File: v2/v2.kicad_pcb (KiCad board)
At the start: 2 copper layers, 9.7 x 8.4 mm, 105 parts, among them J1 Conn_01x04_Pin, J2 Conn_01x04_Pin, J3 Conn_01x04_Pin, SW1 SW_Push, SW10 SW_Push, SW11 SW_Push, SW12 SW_Push, SW13 SW_Push, SW14 SW_Push, SW15 SW_Push, SW16 SW_Push, SW17 SW_Push, SW18 SW_Push, SW19 SW_Push, SW2 SW_Push, SW20 SW_Push, SW21 SW_Push, SW22 SW_Push, SW23 SW_Push, SW24 SW_Push, SW25 SW_Push, SW26 SW_Push, SW27 SW_Push, SW28 SW_Push, SW29 SW_Push, SW3 SW_Push, SW30 SW_Push, SW31 SW_Push, SW32 SW_Push, SW33 RotaryEncoder_Switch, SW4 SW_Push, SW5 SW_Push, SW6 SW_Push, SW7 SW_Push, SW8 SW_Push, SW9 SW_Push, U1 Pico, U2 Pico

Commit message: started running traces
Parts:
- moved U1 4.67 mm to (257.7, 122.0)
- moved U2 4.67 mm to (257.7, 122.0)
- moved J2 4.67 mm to (259.4, 155.9)
- moved J1 4.67 mm to (254.9, 155.7)
- moved R3 4.67 mm to (271.4, 146.1)
- moved R4 4.67 mm to (271.6, 133.7)
- moved J3 3.90 mm to (279.7, 182.8)
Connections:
- D2 pad 1: Net-(D2-K) -> Row 1
- D3 pad 1: Net-(D2-K) -> Row 1
- D4 pad 1: Net-(D2-K) -> Row 1
- D5 pad 1: Net-(D2-K) -> Row 1
- D6 pad 1: Net-(D2-K) -> Row 1
- D7 pad 1: Net-(D2-K) -> Row 1
- U1 pad 31: unconnected-(U1-GPIO26_ADC0-Pad31) -> ENC B
- U1 pad 32: unconnected-(U1-GPIO27_ADC1-Pad32) -> ENC A
- U1 pad 36: unconnected-(U1-3V3-Pad36) -> +3.3V
- U2 pad 24: unconnected-(U2-GPIO18-Pad24) -> SERIAL B
- U2 pad 25: unconnected-(U2-GPIO19-Pad25) -> SERIAL A
- U2 pad 31: unconnected-(U2-GPIO26_ADC0-Pad31) -> ENC B
- U2 pad 32: unconnected-(U2-GPIO27_ADC1-Pad32) -> ENC A
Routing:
- net Row 5: track 0.00 -> 146.9 mm, vias 0 -> 1
- net Row 2: track 0.00 -> 125.6 mm, vias 0 -> 1
- net Row 3: track 0.00 -> 125.3 mm, vias 0 -> 1
- net Row 4: track 0.00 -> 125.1 mm, vias 0 -> 1
- net Col 7: track 0.00 -> 104.7 mm, vias 0 -> 1
- net Col 4: track 0.00 -> 102.4 mm, vias 0 -> 1
- net Col 6: track 0.00 -> 101.8 mm, vias 0 -> 1
- net Row 1: track 0.00 -> 101.0 mm, vias 0 -> 1
- net GND: track 0.00 -> 100.2 mm, vias 0 -> 1
- net Col 2: track 0.00 -> 99.8 mm, vias 0 -> 1
- net Col 5: track 0.00 -> 98.8 mm, vias 0 -> 1
- net Col 3: track 0.00 -> 97.3 mm, vias 0 -> 1
- net Col 1: track 0.00 -> 81.8 mm, vias 0 -> 1
- net +3.3V: track 0.00 -> 47.4 mm, vias 0 -> 1
- net Net-(D6-A): track 0.00 -> 13.8 mm
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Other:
- board size 9.7 x 8.4 mm -> 170.5 x 144.8 mm

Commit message: done for tonight, more trace routing
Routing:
- net Col 1: track 81.8 -> 231.3 mm
- net Col 2: track 99.8 -> 205.2 mm
- net Col 3: track 97.3 -> 185.9 mm
- net Col 4: track 102.4 -> 168.3 mm
- net Col 5: track 98.8 -> 146.0 mm
- net Col 6: track 101.8 -> 122.4 mm
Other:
- outline, holes or cut-outs redrawn

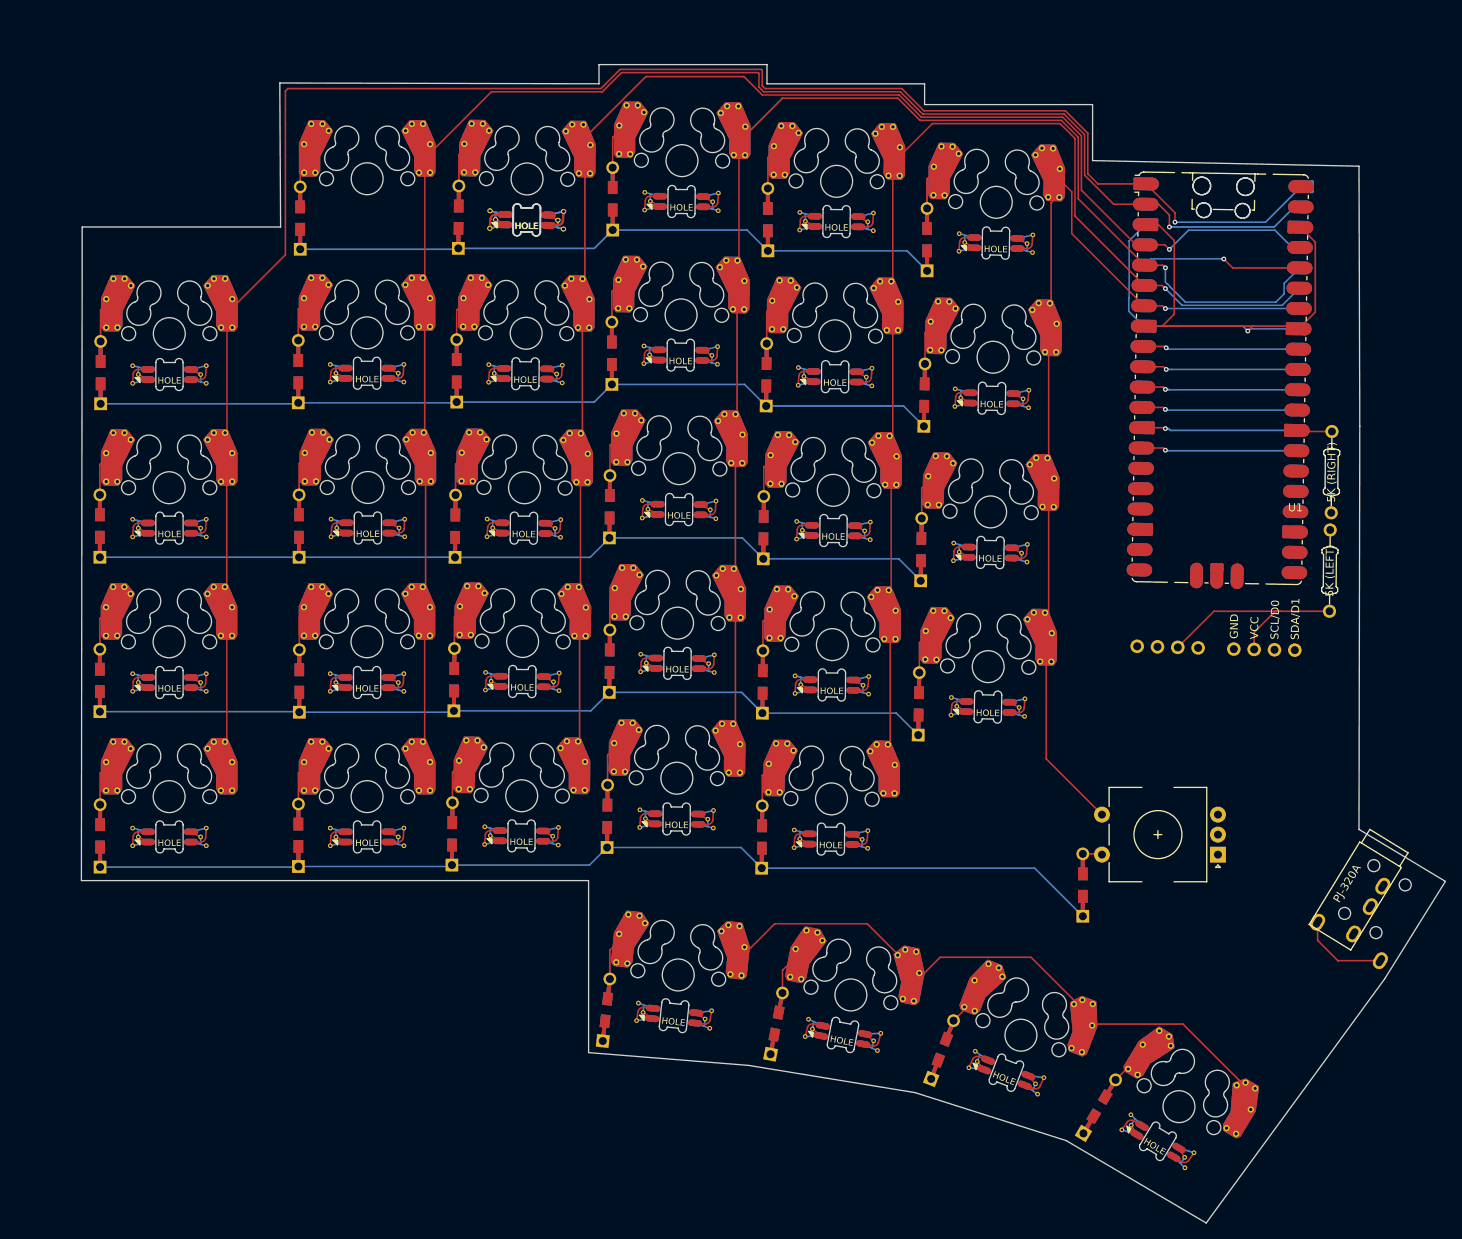
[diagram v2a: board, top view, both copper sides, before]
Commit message: redo some schematics, time to redo LEDs
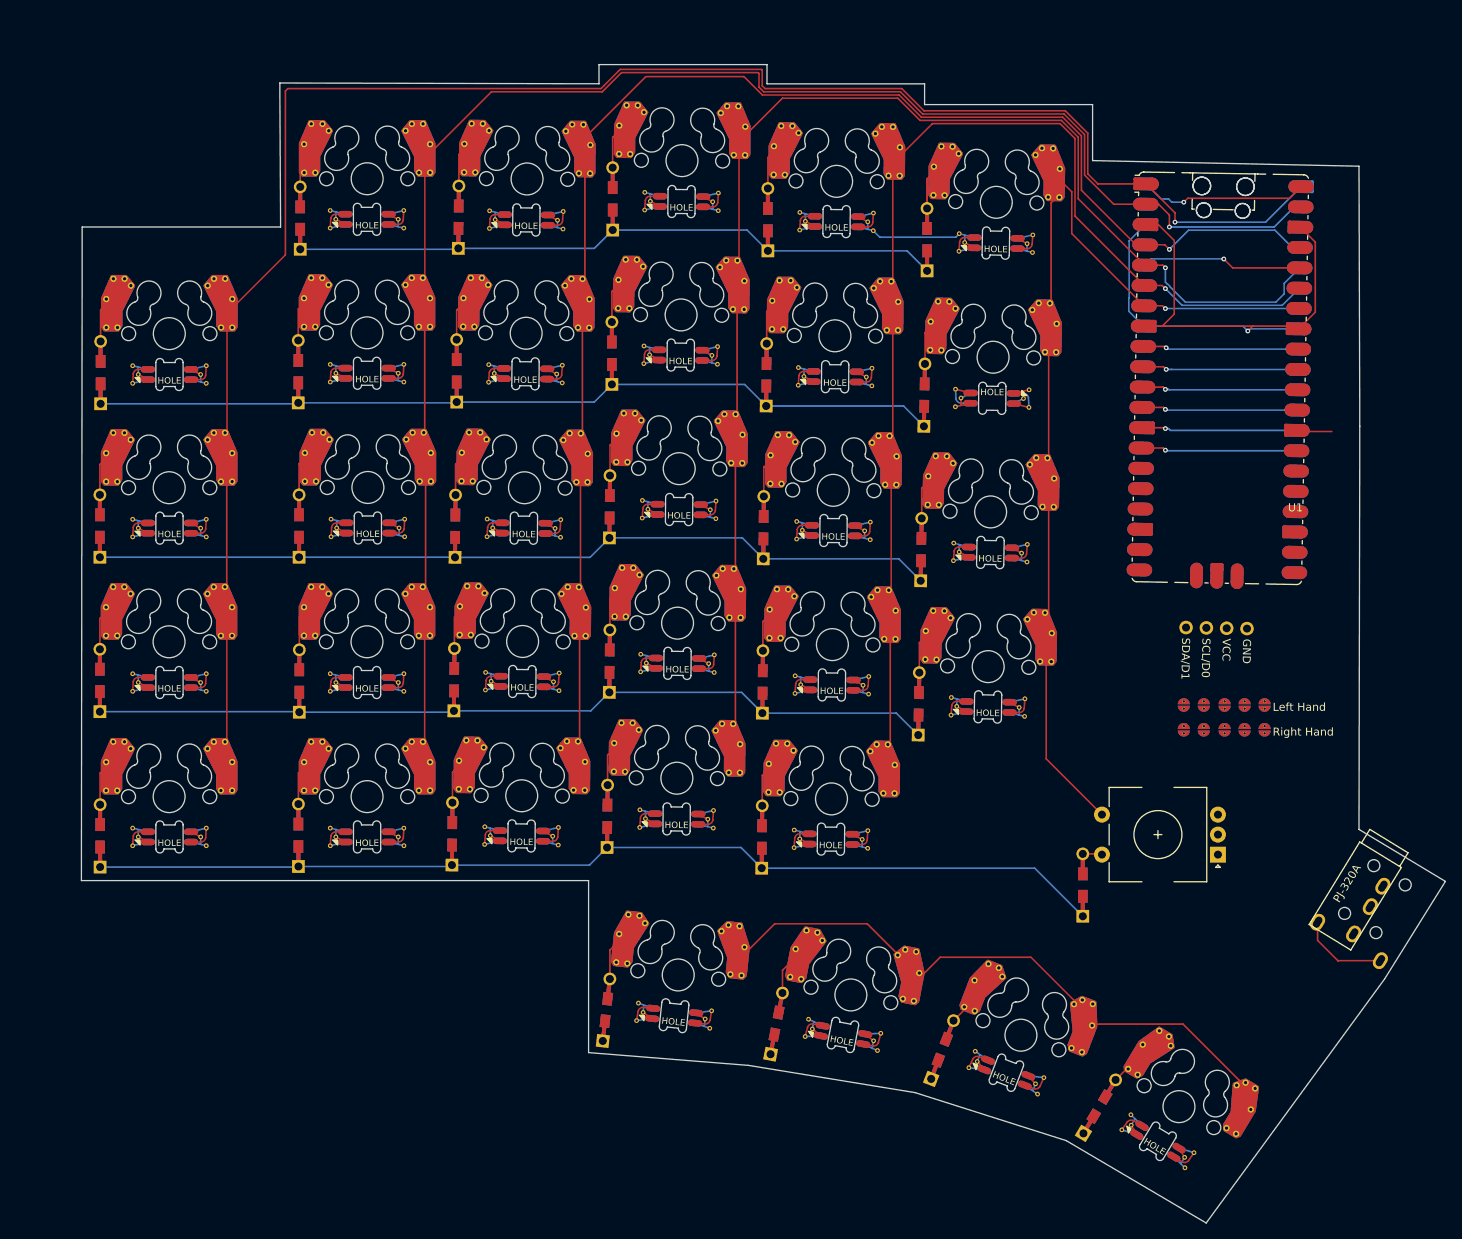
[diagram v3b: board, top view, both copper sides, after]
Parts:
- removed J1: Conn_01x04_Pin, Keebio-Parts:I2C_Breakout
- removed R3: 5K (LEFT), Keebio-Parts:Resistor
- removed R4: 5K (RIGHT), Keebio-Parts:Resistor
- added JP1: GND, Keebio-Parts:solder_jumper, F.Cu at (253.1, 165.9)
- added JP10: Left, Keebio-Parts:solder_jumper, F.Cu at (263.2, 165.9)
- added JP2: VCC, Keebio-Parts:solder_jumper, F.Cu at (255.6, 165.9)
- added JP3: SCL, Keebio-Parts:solder_jumper, B.Cu at (255.6, 162.8)
- added JP4: SDA, Keebio-Parts:solder_jumper, F.Cu at (260.7, 165.9)
- added JP5: SDA, Keebio-Parts:solder_jumper, B.Cu at (253.1, 162.8)
- added JP6: SCL, Keebio-Parts:solder_jumper, F.Cu at (258.2, 165.9)
- added JP7: VCC, Keebio-Parts:solder_jumper, B.Cu at (258.2, 162.8)
- added JP8: GND, Keebio-Parts:solder_jumper, B.Cu at (260.7, 162.8)
- added JP9: Right, Keebio-Parts:solder_jumper, F.Cu at (263.2, 162.8)
- LED13: moved to B.Cu
- moved LED2 20.1 mm to (151.0, 97.1), turned to 0 degrees
- moved J2 3.04 mm to (261.0, 153.3), turned to -91 degrees
- turned LED13 to 179.5 degrees
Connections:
- J2 pad 1: GND -> Net-(J2-Pin_1)
- J2 pad 2: +3.3V -> Net-(J2-Pin_2)
- J2 pad 3: SCL -> Net-(J2-Pin_3)
- J2 pad 4: SCA -> Net-(J2-Pin_4)
- LED30 pad 1: unconnected-(LED30-DOUT-Pad1) -> Net-(LED30-DOUT)
- LED31 pad 3: unconnected-(LED31-DIN-Pad3) -> Net-(LED30-DOUT)
- U1 pad 26: unconnected-(U1-GPIO20-Pad26) -> SDA
- U1 pad 27: unconnected-(U1-GPIO21-Pad27) -> SDL
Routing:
- net +3.3V: track 47.4 -> 20.2 mm
- net VBUS: track 0.00 -> 21.1 mm, vias 0 -> 1
- net Net-(LED5-DOUT): track 0.00 -> 11.3 mm
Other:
- board text added: "Left Hand"
- board text added: "Right Hand"

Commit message: fix LED placement
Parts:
- moved LED6 104.7 mm to (126.3, 116.4), turned to 0 degrees
- moved LED7 89.2 mm to (151.1, 116.3), turned to 0 degrees
- moved LED12 85.4 mm to (126.2, 135.7), turned to 0 degrees
- moved LED22 85.0 mm to (209.2, 155.3), turned to -0.5 degrees
- moved LED13 79.8 mm to (151.1, 135.7), turned to 180 degrees
- moved LED23 77.7 mm to (228.6, 158.0), turned to -1 degrees
- moved LED14 75.4 mm to (170.6, 135.7), turned to -0.5 degrees
- moved LED18 67.4 mm to (126.2, 155.0), turned to 0 degrees
- moved LED15 67.3 mm to (190.0, 133.3), turned to -0.5 degrees
- moved LED21 67.0 mm to (189.8, 152.6), turned to -0.5 degrees
- moved LED19 61.4 mm to (151.0, 155.0), turned to 0 degrees
- moved LED20 60.7 mm to (170.5, 154.9), turned to -0.5 degrees
- moved LED17 58.4 mm to (229.0, 138.7), turned to -1 degrees
- moved LED16 58.2 mm to (209.3, 136.0), turned to -0.5 degrees
- moved LED32 58.1 mm to (252.5, 213.1), turned to -31 degrees
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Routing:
- net Net-(LED5-DOUT): track 11.3 -> 0.00 mm
- net Net-(LED4-DOUT): track 0.00 -> 11.3 mm
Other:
- outline, holes or cut-outs redrawn
